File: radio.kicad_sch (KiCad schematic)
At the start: 23 parts, among them J1 Conn_Coaxial, U11 LC76G, U13 SA818S, U23 E22-900M30S, U24 E22-170M30S

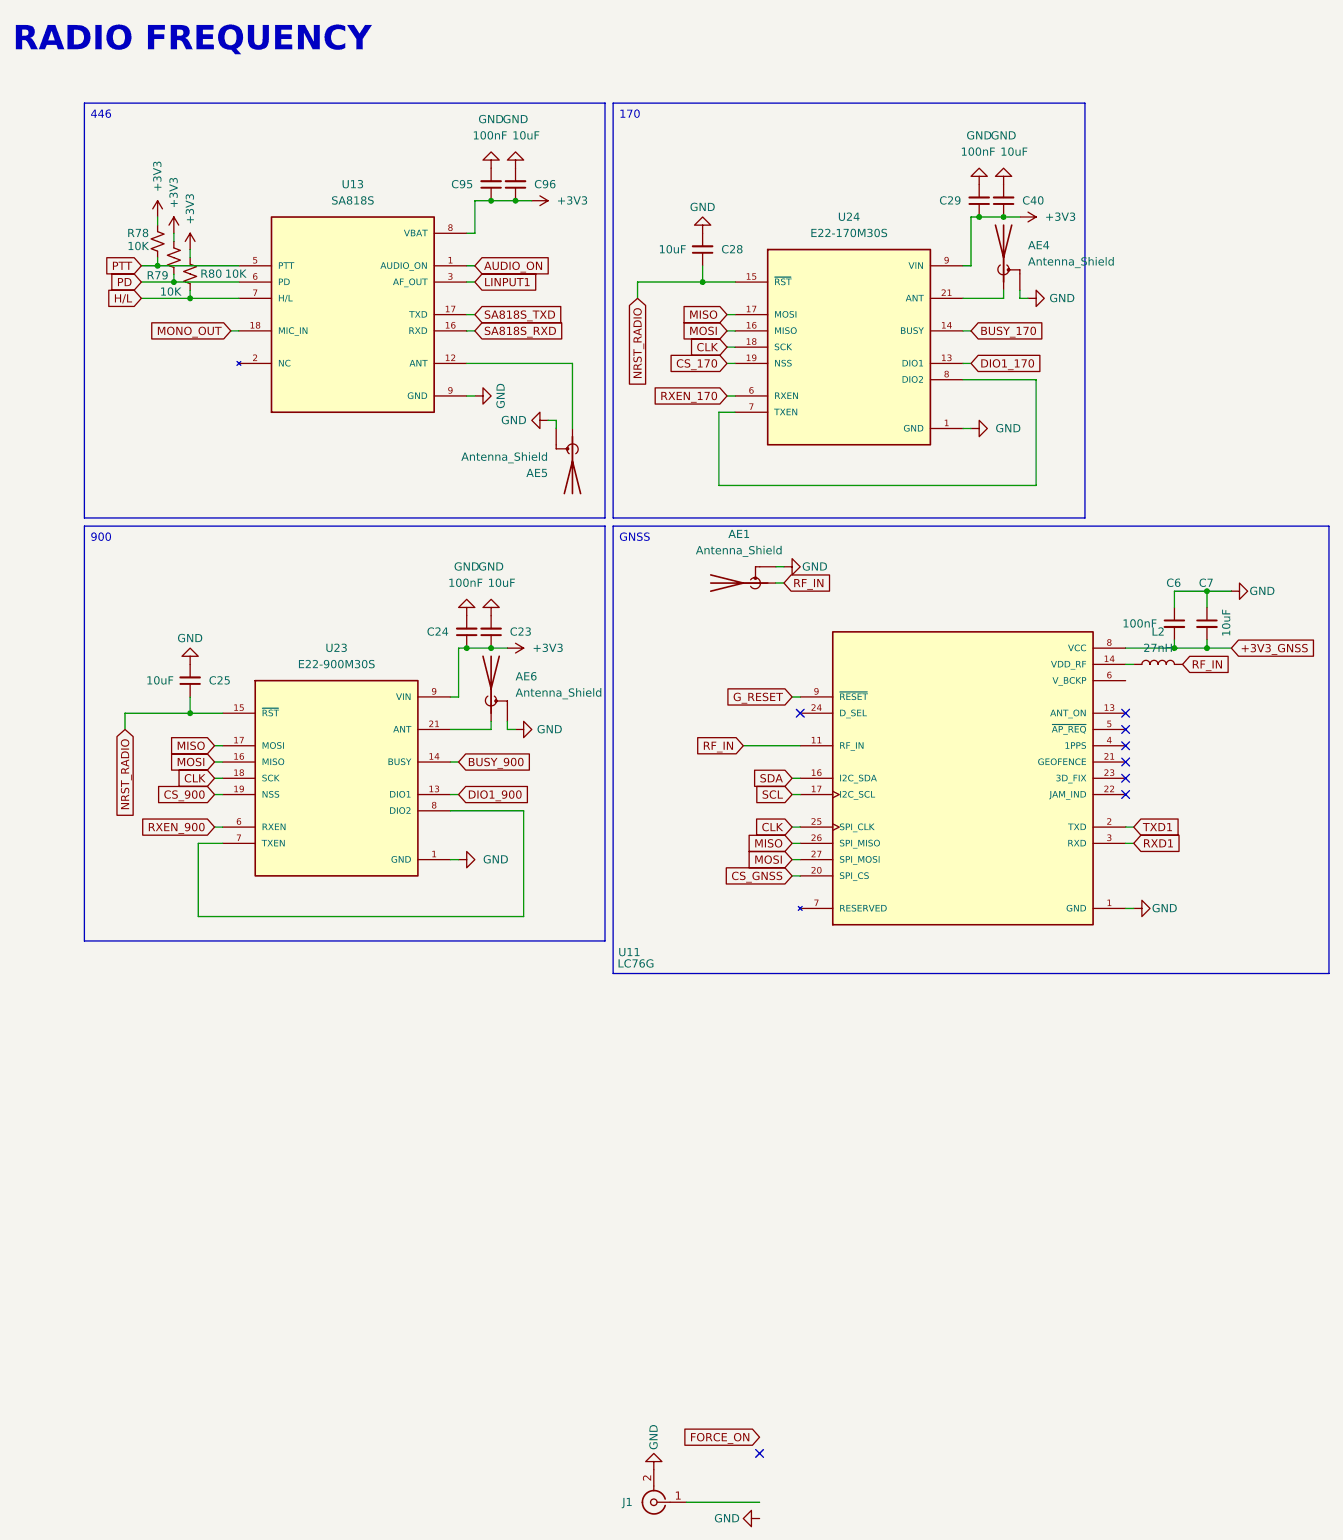
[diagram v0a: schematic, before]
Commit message: Routed RF Core
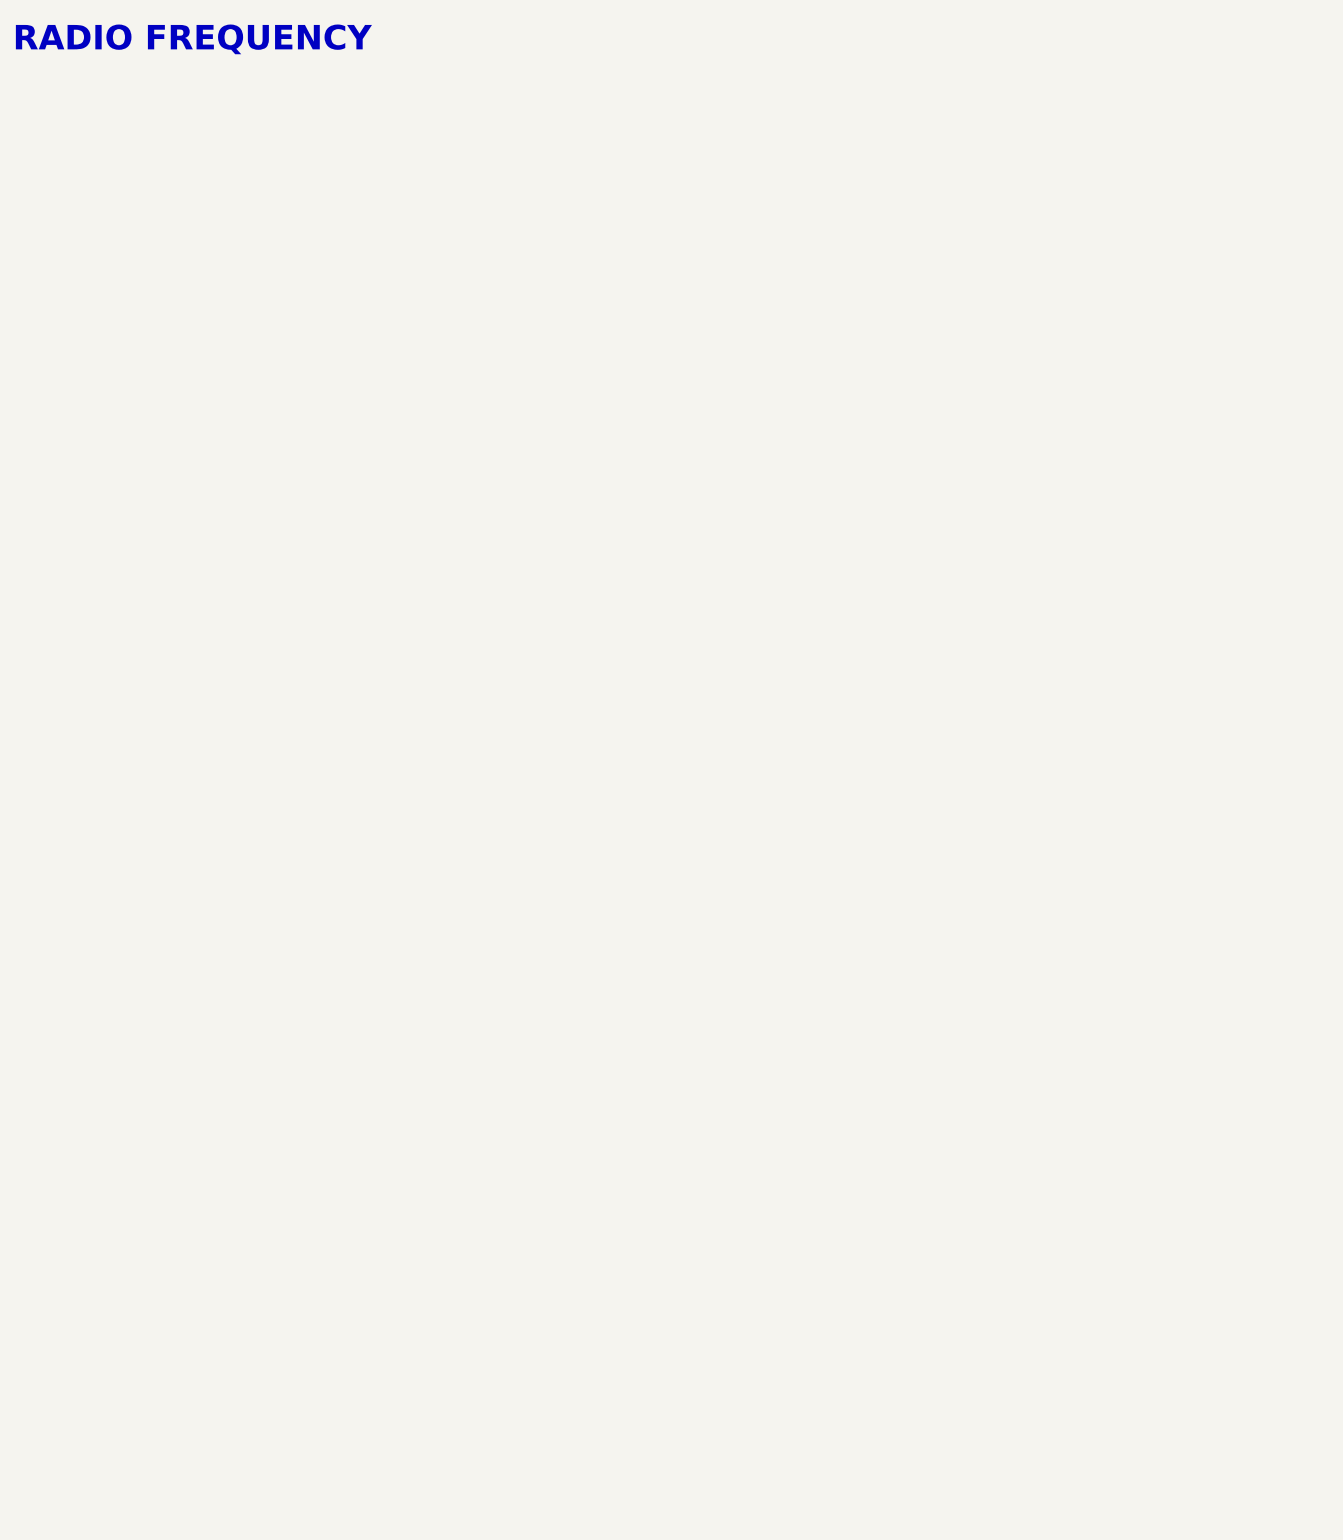
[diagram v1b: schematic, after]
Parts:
- removed AE1: Antenna_Shield, Connector_Coaxial:U.FL_Molex_MCRF_73412-0110_Vertical, symbol Device:Antenna_Shield
- removed AE4, AE5, AE6: Antenna_Shield, Connector_Coaxial:SMA_Amphenol_132289_EdgeMount, symbol Device:Antenna_Shield
- removed C23, C25, C28, C40, C7, C96: 10uF, Capacitor_SMD:C_0603_1608Metric, symbol Device:C_Small
- removed C24, C29, C6, C95: 100nF, Capacitor_SMD:C_0603_1608Metric, symbol Device:C_Small
- removed J1: Conn_Coaxial, Connector_Coaxial:U.FL_Molex_MCRF_73412-0110_Vertical, symbol Connector:Conn_Coaxial
- removed L2: 27nH, symbol Device:L
- removed R78, R79, R80: 10K, Resistor_SMD:R_0603_1608Metric, symbol Device:R_Small_US
- removed U11: LC76G, PTCR:XCVR_LC76G, symbol PTCR-V5:LC76G
- removed U13: SA818S, PTCR:XCVR_SA818S, symbol PTCR-V5:SA818S
- removed U23: E22-900M30S, PTCR:XCVR_E22-900M30S, symbol PTCR-V5:E22-900M30S
- removed U24: E22-170M30S, PTCR:XCVR_E22-900M30S, symbol PTCR-V5:E22-900M30S
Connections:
- no-connect marks 8 -> 0
